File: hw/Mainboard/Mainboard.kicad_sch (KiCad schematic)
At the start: 0 parts

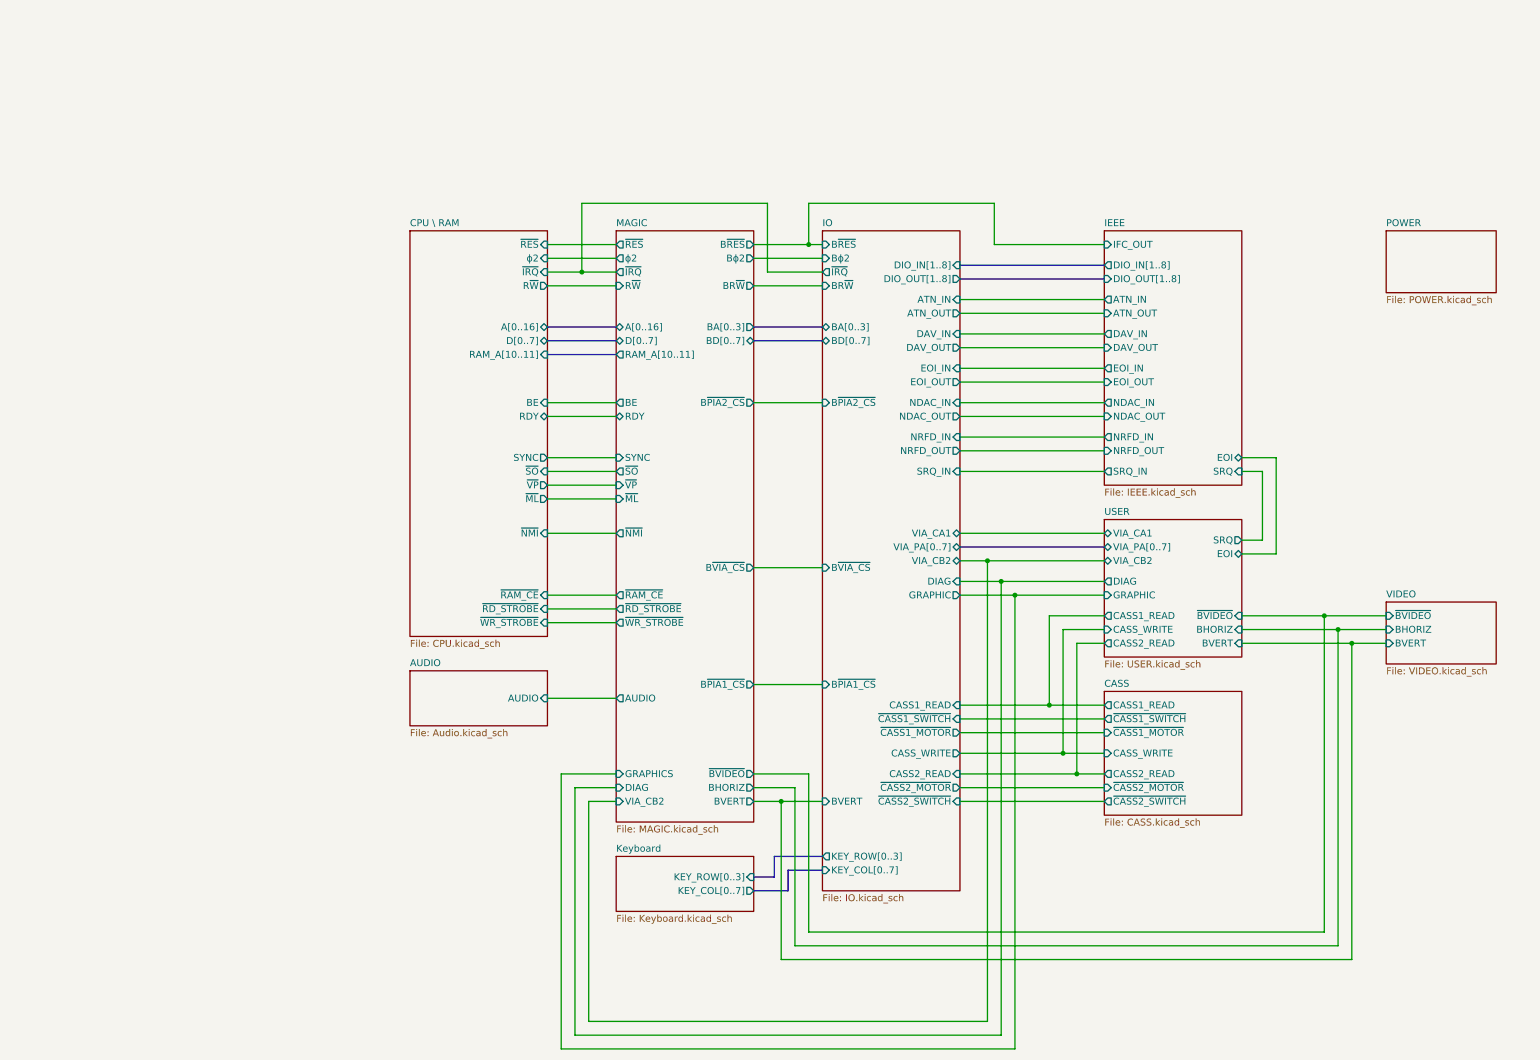
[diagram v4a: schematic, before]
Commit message: hw: tidy power and resize pages
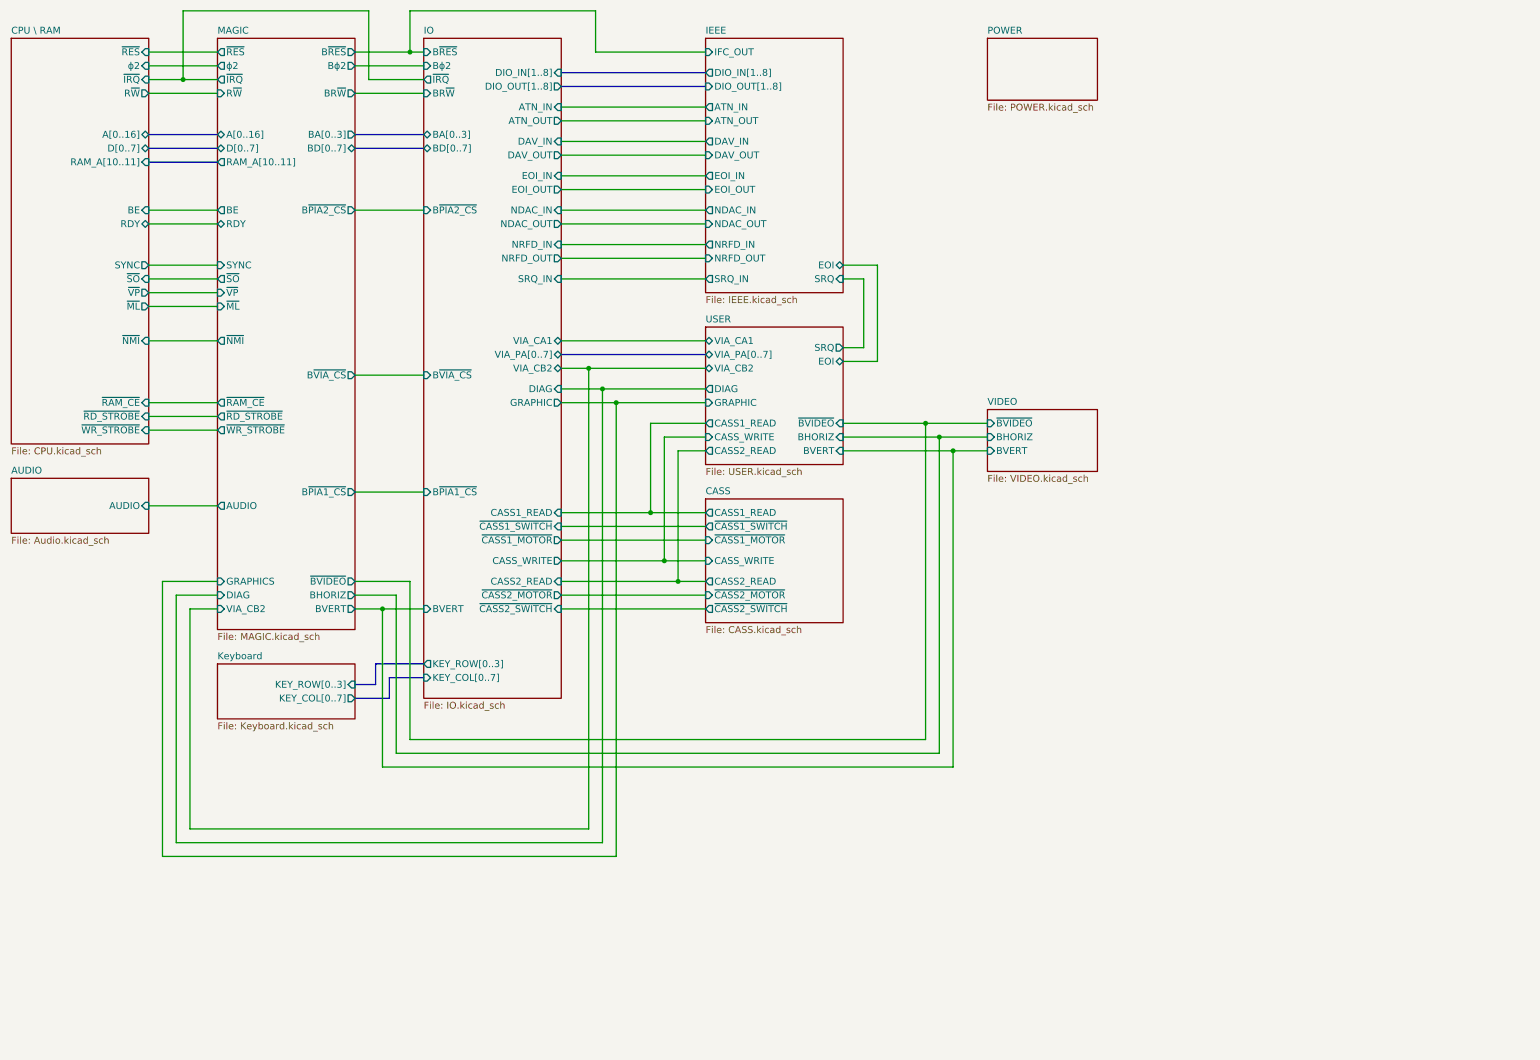
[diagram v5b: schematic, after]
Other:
- title: PET Clone -> CBM PET Mainboard Replacement

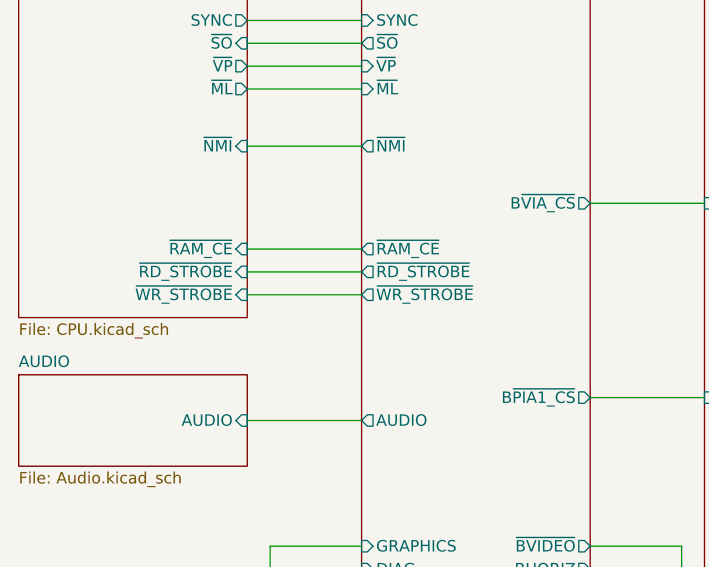
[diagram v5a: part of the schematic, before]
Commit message: hw: tidy CPU, rename RD/WR strobe to RAM_OE/_WE, debounce switches
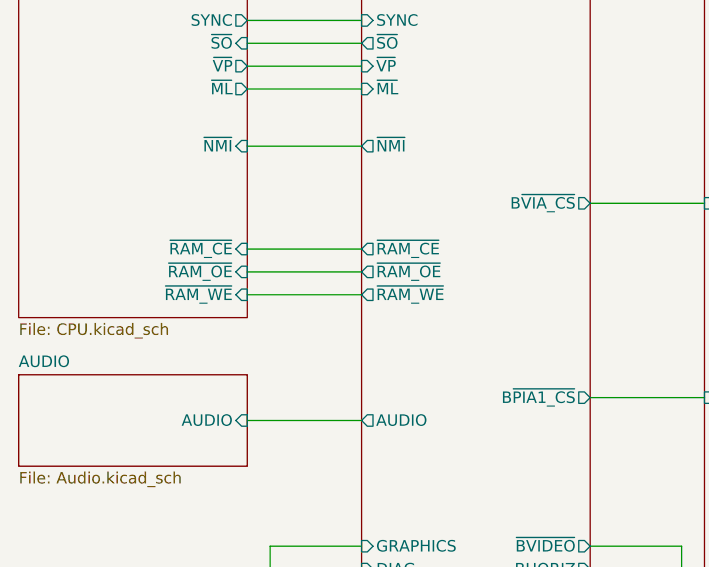
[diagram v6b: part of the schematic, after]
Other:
- sheet CPU \ RAM ports: added ~{RAM_OE}, ~{RAM_WE}; removed ~{RD_STROBE}, ~{WR_STROBE}
- sheet MAGIC ports: added ~{RAM_OE}, ~{RAM_WE}; removed ~{RD_STROBE}, ~{WR_STROBE}
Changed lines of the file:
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@@
       (effects (font (size 1.27 1.27)) (justify right))
     )
-    (pin "~{RD_STROBE}" input (at 66.04 99.06 0)
-      (effects (font (size 1.27 1.27)) (justify right))
-    )
-    (pin "~{WR_STROBE}" input (at 66.04 101.6 0)
+    (pin "~{RAM_OE}" input (at 66.04 99.06 0)
+      (effects (font (size 1.27 1.27)) (justify right))
+    )
+    (pin "~{RAM_WE}" input (at 66.04 101.6 0)
       (effects (font (size 1.27 1.27)) (justify right))
     )
@@
       (effects (font (size 1.27 1.27)) (justify left))
     )
-    (pin "~{RD_STROBE}" output (at 78.74 99.06 180)
-      (effects (font (size 1.27 1.27)) (justify left))
-    )
-    (pin "~{WR_STROBE}" output (at 78.74 101.6 180)
+    (pin "~{RAM_OE}" output (at 78.74 99.06 180)
+      (effects (font (size 1.27 1.27)) (justify left))
+    )
+    (pin "~{RAM_WE}" output (at 78.74 101.6 180)
       (effects (font (size 1.27 1.27)) (justify left))
     )
@@
       (reference "#PWR069") (unit 1) (value "GND") (footprint "")
     )
+    (path "/00000000-0000-0000-0000-0000614e685e/bb600181-08e3-4816-a030-dc9fcb9bd0ce"
+      (reference "#PWR070") (unit 1) (value "+3V3") (footprint "")
+    )
     (path "/00000000-0000-0000-0000-0000617d6918/b70241ab-8a5c-42d5-a1ab-8f4bc50a1197/87920f6c-0e61-4854-aae5-a669432dd717"
       (reference "#PWR071") (unit 1) (value "+3V3") (footprint "")
@@
       (reference "#PWR073") (unit 1) (value "GND") (footprint "")
     )
+    (path "/00000000-0000-0000-0000-0000614e685e/7c864946-0b76-4ecc-9f68-a527ea960ef3"
+      (reference "#PWR074") (unit 1) (value "+3V3") (footprint "")
+    )
+    (path "/00000000-0000-0000-0000-0000614e685e/7dae687a-8430-485d-aa7f-e7ff5af76271"
+      (reference "#PWR075") (unit 1) (value "GND") (footprint "")
+    )
+    (path "/00000000-0000-0000-0000-0000614e685e/9f547c85-89fe-4802-9cd1-c433da2c659b"
+      (reference "#PWR076") (unit 1) (value "GND") (footprint "")
+    )
     (path "/00000000-0000-0000-0000-0000617d6918/b70241ab-8a5c-42d5-a1ab-8f4bc50a1197/f746e1f0-8bed-49ea-84ec-400629af52a7"
       (reference "#PWR077") (unit 1) (value "GND") (footprint "")
     )
+    (path "/00000000-0000-0000-0000-0000614e685e/517d69ba-9230-4b63-b2e0-1b097d2a5d99"
+      (reference "#PWR078") (unit 1) (value "GND") (footprint "")
+    )
     (path "/00000000-0000-0000-0000-0000617d6918/b70241ab-8a5c-42d5-a1ab-8f4bc50a1197/6cb354c4-9c1d-443a-a923-db91f3a77286"
       (reference "#PWR079") (unit 1) (value "GND") (footprint "")
@@
       (reference "#PWR084") (unit 1) (value "+3V3") (footprint "")
     )
+    (path "/00000000-0000-0000-0000-0000614e685e/bb09ef57-d37f-4b12-bcd2-7c4861f6b046"
+      (reference "#PWR085") (unit 1) (value "GND") (footprint "")
+    )
     (path "/00000000-0000-0000-0000-0000617d6918/b70241ab-8a5c-42d5-a1ab-8f4bc50a1197/baea8478-1e02-497f-88d9-4b0c6c77bc0e"
       (reference "#PWR086") (unit 1) (value "GND") (footprint "")
@@
       (reference "#PWR0126") (unit 1) (value "GND") (footprint "")
     )
-    (path "/00000000-0000-0000-0000-0000614e685e/553376f0-e008-49a0-9203-113849368f6d"
-      (reference "#PWR0127") (unit 1) (value "PD_3V3") (footprint "")
-    )
     (path "/00000000-0000-0000-0000-0000614e685e/df1b28fc-a4b9-450d-972a-836a9e2c70b9"
       (reference "#PWR0128") (unit 1) (value "GND") (footprint "")
@@
       (reference "#PWR0135") (unit 1) (value "PD_6V") (footprint "")
     )
-    (path "/00000000-0000-0000-0000-0000614e685e/1ddaf6cc-aa3f-4aed-90d7-91f2d49f7bb4"
-      (reference "#PWR0136") (unit 1) (value "PD_GND") (footprint "")
-    )
-    (path "/00000000-0000-0000-0000-0000617d6918/20dbd71a-f964-4c21-a5bf-ad81adee599f"
-      (reference "#PWR0141") (unit 1) (value "PD_GND") (footprint "")
-    )
-    (path "/00000000-0000-0000-0000-0000614e685e/b62b6061-2d7c-480a-ac77-eac075043940"
-      (reference "#PWR0143") (unit 1) (value "PD_3V3") (footprint "")
-    )
     (path "/00000000-0000-0000-0000-000061ed99de/643c3bdf-7270-415a-a261-9d67a30bfd21"
       (reference "#PWR0155") (unit 1) (value "GND") (footprint "")
@@
       (reference "#PWR0158") (unit 1) (value "PD_5V") (footprint "")
     )
-    (path "/00000000-0000-0000-0000-0000617d6918/f3557c31-99ab-4007-9ad4-ebce5681b427"
-      (reference "#PWR0159") (unit 1) (value "PD_GND") (footprint "")
-    )
     (path "/00000000-0000-0000-0000-000061a7d9c6/833f676c-97a5-42f1-b79a-7d5bf5a6df79"
       (reference "#PWR0166") (unit 1) (value "PD_GND") (footprint "")
@@
       (reference "#PWR0197") (unit 1) (value "PD_6V") (footprint "")
     )
-    (path "/00000000-0000-0000-0000-0000614e685e/1013e2be-f9cc-42da-90d1-29ea445af089"
-      (reference "#PWR0198") (unit 1) (value "PD_GND") (footprint "")
-    )
     (path "/00000000-0000-0000-0000-000061b9c2eb/e8232aba-4b8a-4c32-9392-0db70a5223e8"
       (reference "#PWR0200") (unit 1) (value "PD_GND") (footprint "")
@@
       (reference "C23") (unit 1) (value "100n") (footprint "Capacitor_SMD:C_0402_1005Metric")
     )
-    (path "/00000000-0000-0000-0000-0000617d6918/00000000-0000-0000-0000-0000636ec979"
-      (reference "C24") (unit 1) (value "100n") (footprint "Capacitor_SMD:C_0402_1005Metric")
-    )
-    (path "/00000000-0000-0000-0000-0000617d6918/00000000-0000-0000-0000-00006384e2d1"
-      (reference "C25") (unit 1) (value "100n") (footprint "Capacitor_SMD:C_0402_1005Metric")
+    (path "/00000000-0000-0000-0000-0000614e685e/5adfbe75-0f57-4bb2-a663-fab6b20ad684"
+      (reference "C24") (unit 1) (value "10u") (footprint "Capacitor_SMD:C_0603_1608Metric")
+    )
+    (path "/00000000-0000-0000-0000-0000614e685e/bc68d6d4-f945-497c-b7a1-b5400016cfe7"
+      (reference "C25") (unit 1) (value "10u") (footprint "Capacitor_SMD:C_0603_1608Metric")
     )
     (path "/00000000-0000-0000-0000-000061ed99de/4a35284c-f82d-4693-8829-24ba7effdf90"
@@
       (reference "C82") (unit 1) (value "100n") (footprint "Capacitor_SMD:C_0402_1005Metric")
     )
-    (path "/00000000-0000-0000-0000-0000617d6918/b70241ab-8a5c-42d5-a1ab-8f4bc50a1197/67b8a916-4b92-4a4a-910a-6fc2db71488c"
-      (reference "C83") (unit 1) (value "100n") (footprint "Capacitor_SMD:C_0402_1005Metric")
-    )
-    (path "/00000000-0000-0000-0000-0000617d6918/b70241ab-8a5c-42d5-a1ab-8f4bc50a1197/89cb9fe8-b0fa-4b02-ae31-04bf78751b16"
-      (reference "C84") (unit 1) (value "100n") (footprint "Capacitor_SMD:C_0402_1005Metric")
+    (path "/00000000-0000-0000-0000-0000617d6918/b70241ab-8a5c-42d5-a1ab-8f4bc50a1197/4bbfc88f-5e22-453e-ac3d-d10fbc3241d7"
+      (reference "C?") (unit 1) (value "10u") (footprint "Capacitor_SMD:C_0603_1608Metric")
+    )
+    (path "/00000000-0000-0000-0000-0000617d6918/b70241ab-8a5c-42d5-a1ab-8f4bc50a1197/cfa2d6f0-341d-4d41-b3a2-79c3476fc073"
+      (reference "C?") (unit 1) (value "1u") (footprint "Capacitor_SMD:C_0402_1005Metric")
     )
     (path "/00000000-0000-0000-0000-000061ed99de/00000000-0000-0000-0000-000061f4c74a"
@@
       (reference "NT21") (unit 1) (value "GND") (footprint "PET:NetTie-2_SMD_Pad_1.6_to_0.4mm")
     )
-    (path "/00000000-0000-0000-0000-0000617d6918/7432ee29-bc7c-480e-a841-5ed07649471f"
-      (reference "NT22") (unit 1) (value "GND") (footprint "PET:NetTie-2_SMD_Pad_1.6_to_0.4mm")
-    )
-    (path "/00000000-0000-0000-0000-0000617d6918/2ecc9ee0-05f6-42aa-af9d-930a8667bdcf"
-      (reference "NT23") (unit 1) (value "GND") (footprint "PET:NetTie-2_SMD_Pad_1.6_to_0.4mm")
-    )
     (path "/5178399f-3ceb-4969-8efa-17e54018f3f1/25b75009-5a0e-436b-a13f-4da44a9ac874"
       (reference "NT24") (unit 1) (value "GND") (footprint "PET:NetTie-2_SMD_Pad_1.6_to_0.4mm")
@@
       (reference "NT44") (unit 1) (value "+3V3") (footprint "PET:NetTie-2_SMD_Pad_0.4_to_0.28mm")
     )
-    (path "/00000000-0000-0000-0000-0000614e685e/94e507f6-735a-4cb0-9142-e0c22efdca88"
-      (reference "PT1") (unit 1) (value "PowerTie_2") (footprint "PET:NetTie-2_SMD_Pad_1.6_to_0.4mm")
-    )
-    (path "/00000000-0000-0000-0000-0000614e685e/d397e821-0519-4d0d-8cad-98db54b872a5"
-      (reference "PT2") (unit 1) (value "PowerTie_2") (footprint "PET:NetTie-2_SMD_Pad_1.6_to_0.4mm")
-    )
     (path "/00000000-0000-0000-0000-0000617d6918/00000000-0000-0000-0000-000062edbe39/6aa3ead0-db98-46a7-b068-13c9e25e3f07"
       (reference "PT3") (unit 1) (value "PowerTie_2") (footprint "PET:NetTie-2_SMD_Pad_1.6_to_0.4mm")
@@
       (reference "RV1") (unit 1) (value "20k") (footprint "Potentiometer_SMD:Potentiometer_Bourns_TC33X_Vertical")
     )
-    (path "/00000000-0000-0000-0000-0000617d6918/d724628a-968b-43f8-8489-f234f074e4df"
+    (path "/00000000-0000-0000-0000-0000614e685e/5ee6957f-f52e-4db3-af27-7a7a95b3577d"
       (reference "SW1") (unit 1) (value "RESET") (footprint "JLCPCB:SW-TH_L6.0-W3.5-P6.50")
     )
@@
       (reference "SW3") (unit 1) (value "MENU") (footprint "JLCPCB:KEY-TH_SKHLLBA010")
     )
-    (path "/00000000-0000-0000-0000-0000617d6918/00000000-0000-0000-0000-00006384e2ca"
+    (path "/00000000-0000-0000-0000-0000614e685e/7bd4b924-fc4a-4291-9b25-4d0181ac2e94"
       (reference "SW4") (unit 1) (value "NMI") (footprint "JLCPCB:SW-TH_L6.0-W3.5-P6.50")
     )
